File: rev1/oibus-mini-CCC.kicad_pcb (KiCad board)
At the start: 2 copper layers, 37 x 60 mm, 81 parts, among them J1 Conn_01x04_Female, J2 USB_B_Micro, J3 uavcan_5pins, J4 Conn_01x02_Female, P1 TC2030-MCP, Q1 DMG3415U-7, Q2 DMG3415U-7, Q3 DMG3415U-7, SW1 SW_Push, U1 AP2112K-3.3, U10 TPD3E001DRLR, U2 SAM-M8Q, U3 NINA-B311-00B, U4 MCP73831-2-OT, U5 MCP1624T, U6 SHT31-DIS-B, U7 TCAN330, U8 STM32F303CCTx, U9 DW01C-G, Y1 16M, Y2 32kHz

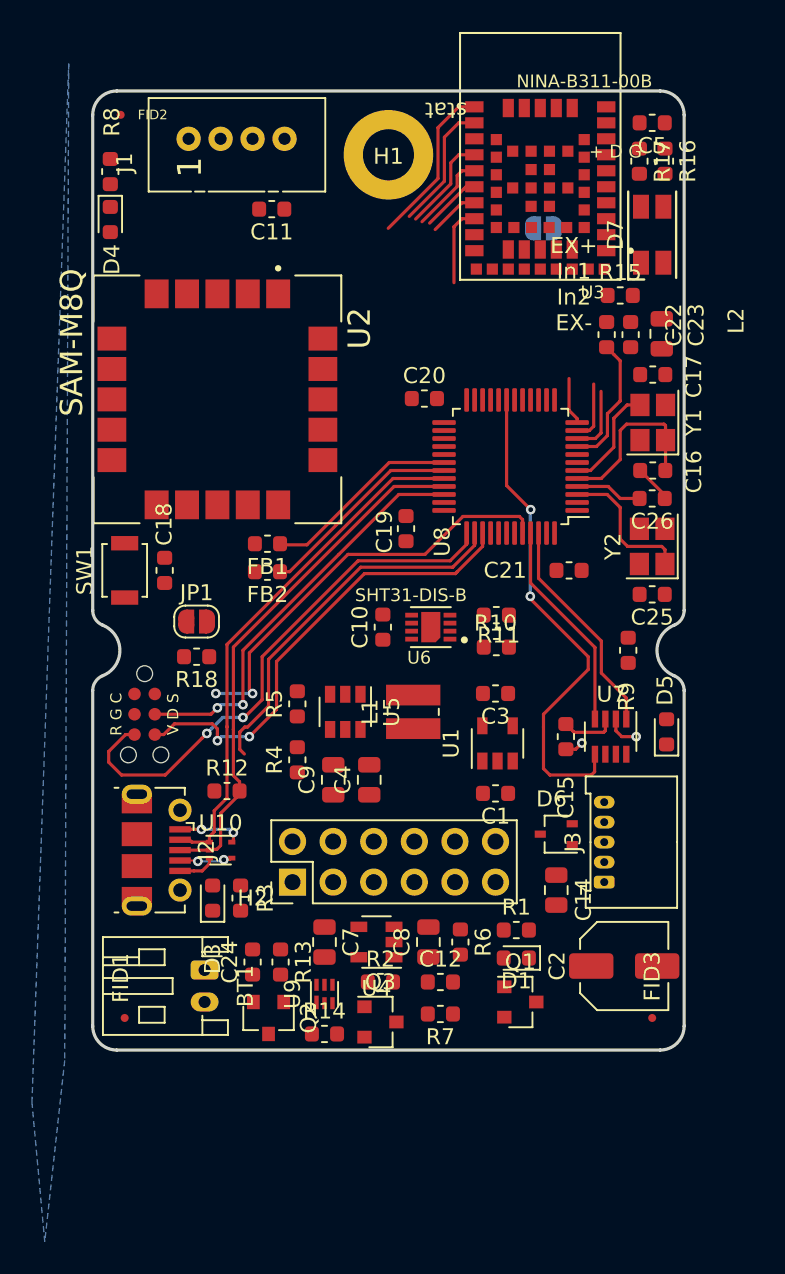
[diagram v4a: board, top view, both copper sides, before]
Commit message: routing halfway done
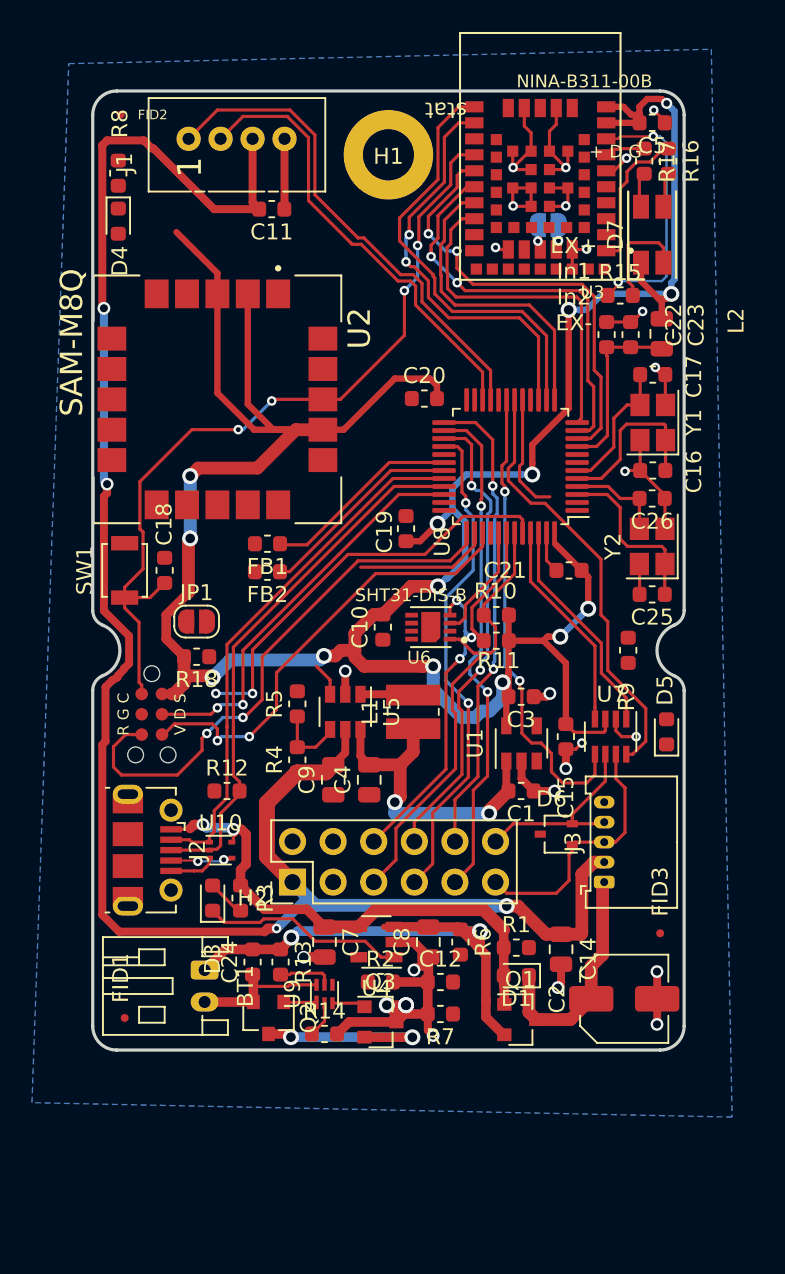
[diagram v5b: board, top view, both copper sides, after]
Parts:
- moved FID3 5.32 mm to (35.5, -7.30)
- moved C14 3.71 mm to (29.3, -6.30)
- moved C2 2.05 mm to (33.2, -3.20)
- moved R10 2.00 mm to (25.2, -27.2)
- moved C3 1.61 mm to (26.8, -22.1)
- moved C1 1.61 mm to (26.8, -16.2)
- moved R11 1.60 mm to (25.2, -25.6)
- moved U1 1.50 mm to (26.8, -19.2)
- moved Q1 1.10 mm to (26.8, -1.90)
- moved D1 1.10 mm to (26.5, -4.65)
- moved R1 1.10 mm to (26.5, -6.40)
- moved J2 0.56 mm to (3.44, -12.5)
- moved D4 0.51 mm to (1.60, -51.9)
- moved R8 0.51 mm to (1.60, -54.9)
- moved P1 0.45 mm to (3.70, -21.0)
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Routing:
- net +3V3: track 3.46 -> 185.2 mm, vias 0 -> 14
- net +5V: track 0.00 -> 118.5 mm, vias 0 -> 4
- net GND: track 8.08 -> 88.0 mm, vias 2 -> 26
- net /~RESET: track 5.91 -> 51.0 mm, vias 0 -> 4
- net /VIN: track 0.00 -> 34.5 mm, vias 0 -> 2
- net +BATT: track 0.00 -> 33.2 mm, vias 0 -> 2
- net /SPI_SCK: track 0.00 -> 31.7 mm, vias 0 -> 2
- net /SPI_MOSI: track 0.00 -> 31.2 mm, vias 0 -> 2
- net /SPS_RX: track 0.00 -> 31.1 mm
- net /~SPI_ADS_CS: track 0.00 -> 29.8 mm, vias 0 -> 2
- net /SPI_MISO: track 0.00 -> 29.5 mm, vias 0 -> 2
- net /SDA: track 0.00 -> 29.3 mm
- net /SPS_TX: track 0.00 -> 28.5 mm
- net VBUS: track 4.06 -> 32.4 mm
- net /SCL: track 0.00 -> 27.7 mm, vias 0 -> 3
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
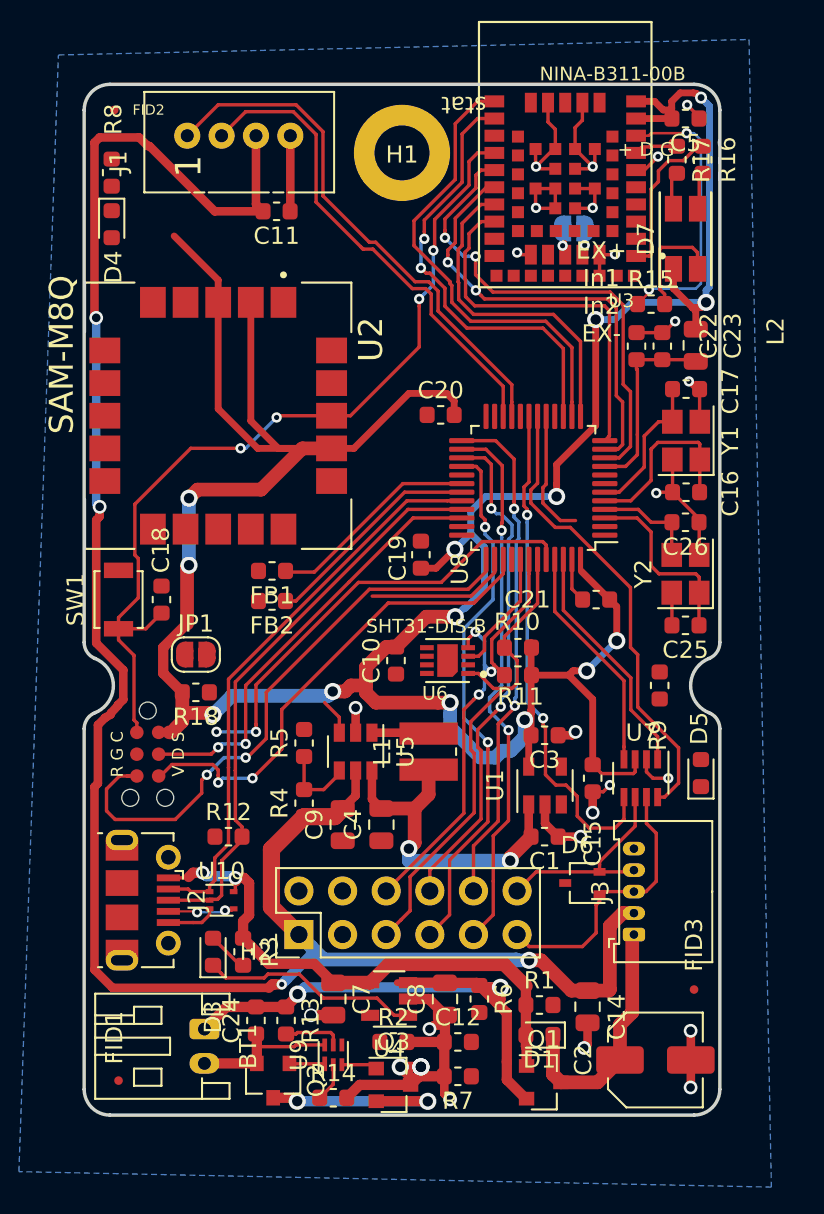
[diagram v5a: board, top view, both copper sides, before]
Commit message: finished routing, DRC clear
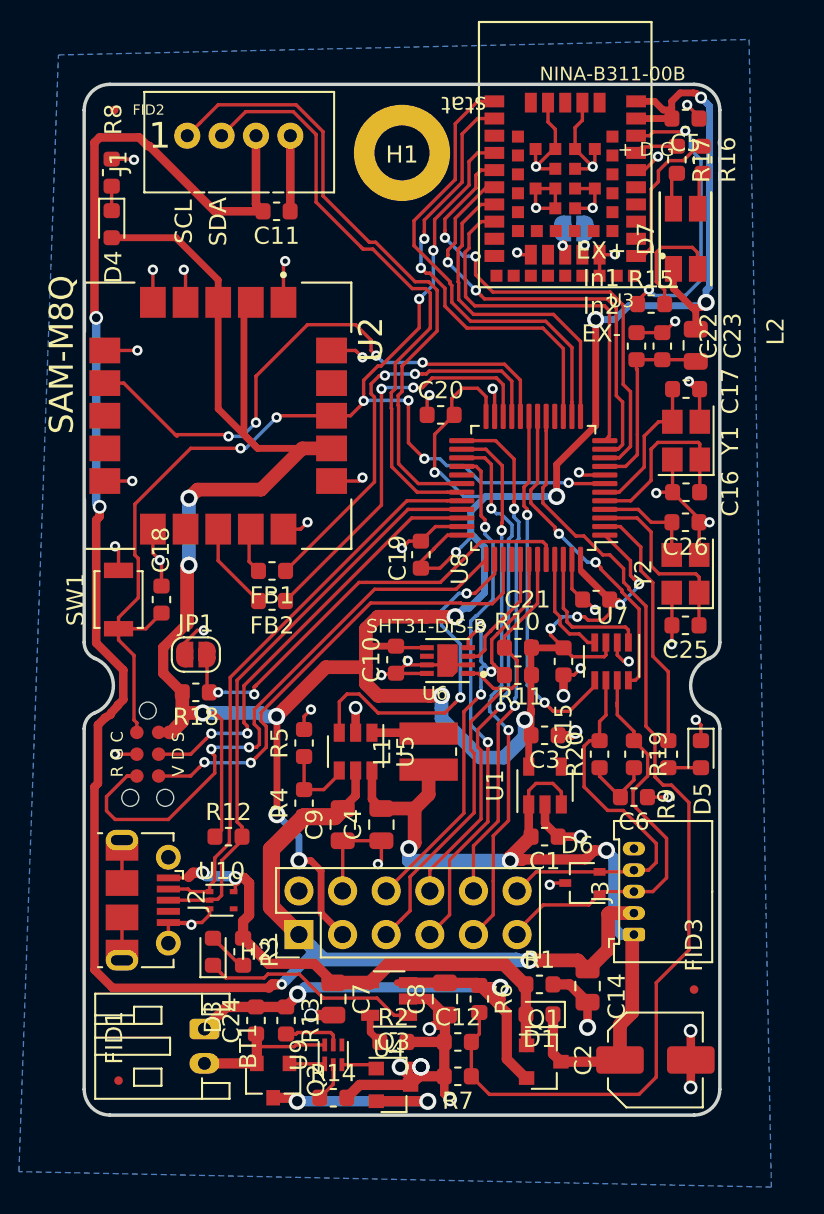
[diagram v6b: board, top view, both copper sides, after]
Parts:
- added C6: 100n, Capacitor_SMD:C_0603_1608Metric, F.Cu at (32.0, -18.5)
- added R19: 60R, Resistor_SMD:R_0603_1608Metric, F.Cu at (32.0, -21.0)
- added R20: 60R, Resistor_SMD:R_0603_1608Metric, F.Cu at (30.0, -21.0)
- moved C15 7.01 mm to (27.9, -26.4)
- moved U7 7.01 mm to (30.7, -26.4)
- moved R9 4.03 mm to (34.0, -21.0)
- moved C14 1.20 mm to (29.3, -7.50)
- moved Q1 1.20 mm to (26.8, -3.10)
- moved D1 1.20 mm to (26.5, -5.85)
- moved R1 1.20 mm to (26.5, -7.60)
- moved D5 1.10 mm to (35.9, -21.0), turned to 270 degrees
- moved C10 0.05 mm to (18.1, -26.5)
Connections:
- J1 pad 1: /SPS_RX -> SPS_RX
- J1 pad 2: /SPS_TX -> SPS_TX
- J2 pad 4: /ID -> (no net)
- U10 pad 4: /ID -> (no net)
- U6 pad 6: /~RESET -> (no net)
- U8 pad 2: (no net) -> /CAN_LED
- U8 pad 21: /SPS_RX -> GPS_RX
- U8 pad 22: /SPS_TX -> GPS_TX
- U8 pad 30: GPS_RX -> SPS_RX
- U8 pad 31: GPS_TX -> SPS_TX
- U8 pad 40: /CAN_LED -> (no net)
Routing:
- net GND: track 88.0 -> 151.8 mm, vias 26 -> 54
- net /BAT_MEAS: track 7.45 -> 59.2 mm
- net SPS_RX: track 0.00 -> 37.2 mm
- net SPS_TX: track 0.00 -> 35.3 mm
- net +3V3: track 185.2 -> 220.2 mm, vias 14 -> 19
- net /GPS_TIME: track 0.00 -> 33.7 mm, vias 0 -> 4
- net /SPS_RX: track 31.1 -> 0.00 mm
- net /SPS_TX: track 28.5 -> 0.00 mm
- net /~RESET: track 51.0 -> 68.6 mm, vias 4 -> 8
- net /VIN: track 34.5 -> 49.6 mm, vias 2 -> 3
- net /CAN_LED: track 0.00 -> 14.5 mm
- net GPS_RX: track 12.4 -> 23.9 mm, vias 0 -> 2
- net GPS_TX: track 12.9 -> 24.0 mm, vias 0 -> 2
- net /CAN_L: track 12.5 -> 22.5 mm
- net /5V_EN: track 10.6 -> 20.2 mm, vias 0 -> 2
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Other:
- board text added: "SCL"
- board text added: "SDA"

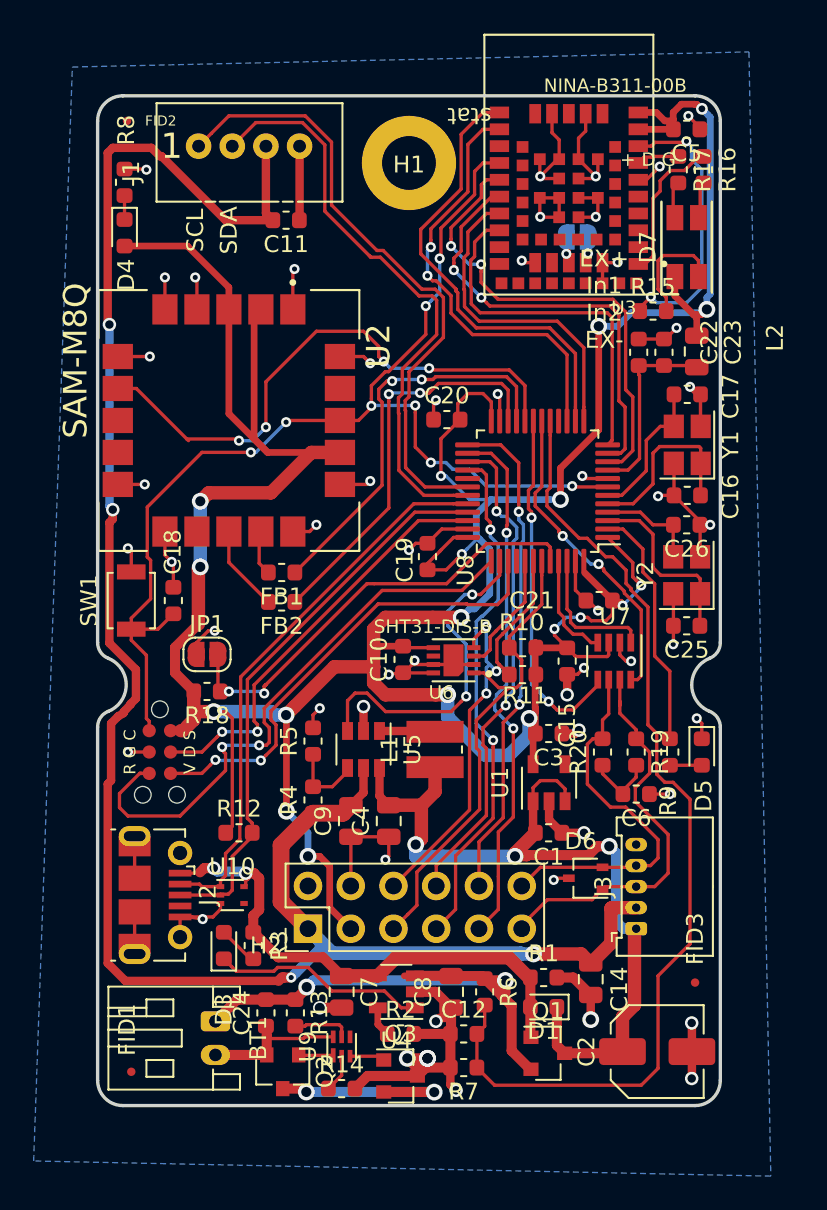
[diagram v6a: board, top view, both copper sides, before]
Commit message: Corrected Silkscreen, added CCC logo, OSH logo, License and revision and other labels
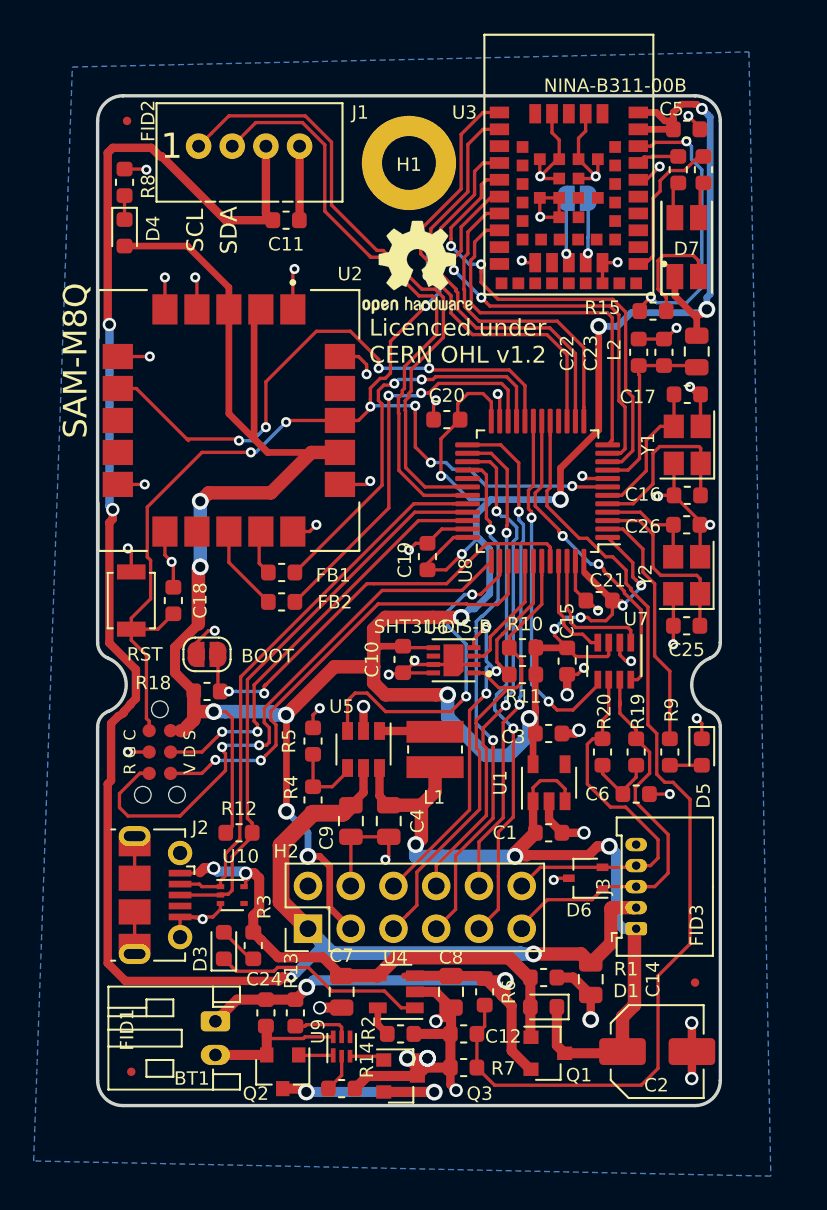
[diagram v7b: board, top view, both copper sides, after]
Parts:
- added G***: LOGO, lib_fp:CCC_logo, B.Cu at (18.1, -44.6)
- added REF**: OSHW-Logo2_7.3x6mm_SilkScreen, Symbol:OSHW-Logo2_7.3x6mm_SilkScreen, F.Cu at (19.0, -49.8)
- moved B1 12.6 mm to (18.9, -20.9)
- moved NFC 2.30 mm to (28.5, -53.9)
- renumbered JP1 to BOOT, J4 to NFC, SW1 to RST
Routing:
- net GND: track 151.8 -> 148.8 mm, vias 54 -> 53
- net Net-(J4-Pad2): track 1.99 -> 4.29 mm
- net Net-(J4-Pad1): track 1.59 -> 3.89 mm
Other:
- board text added: "5V"
- board text added: "<<MCU >>MCU"
- board text added: "Air Quality Sensor Board Made with KiCAD by Octanis Instruments OÜ www.octanis.ch"
- board text added: "BAT+"
- board text added: "GND"
- board text added: "GPS"
- board text added: "Licenced under CERN OHL v1.2"
- board text added: "Rev 1, 10.2019, RT For research purposes only, not approved for resale."
- board text added: "SPS30"
- board text added: "THE CLIMATE CITY CUP"
- board text removed: "+ D G"
- board text removed: "EX+ In1 In2 EX-"
- board text removed: "For prototyping purposes only, not approved for resale."
- board text removed: "OIBUS-Mini Load Cell Module Rev 1, 7.2019, RT Octanis Instruments OÜ www.octanis.ch"
- board text removed: "stat"
- board text removed: "← TagConnect SWD"

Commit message: performed some last fixes. Ready to review
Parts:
- removed BOOT: Jumper_NO_Small, Jumper:SolderJumper-2_P1.3mm_Open_RoundedPad1.0x1.5mm
- removed RST: SW_Push, Button_Switch_SMD:SW_SPST_B3U-1000P
- added SW1: SW_Push, Button_Switch_SMD:SW_SPST_B3U-1000P, F.Cu at (2.00, -30.0)
- D1: footprint Diode_SMD:D_0603_1608Metric -> Diode_SMD:D_SOD-123F
- Q2, Q3: value DMG3415U-7 -> NMOS
- moved R18 3.86 mm to (5.40, -28.3), turned to 0 degrees
- moved C18 3.52 mm to (5.40, -26.6), turned to 0 degrees
- moved C14 2.70 mm to (29.2, -10.2)
- moved D1 0.78 mm to (27.2, -5.50)
- moved Q1 0.70 mm to (26.8, -2.40)
- renumbered NFC to J4
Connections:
- Q3 pad 2: Net-(Q2-Pad3) -> GND
- Q3 pad 3: GND -> Net-(Q2-Pad3)
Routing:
- net +BATT: track 32.0 -> 39.3 mm
- net /BOOT: track 26.9 -> 34.2 mm
- net GND: track 148.8 -> 154.2 mm, vias 53 -> 56
- net Net-(Q2-Pad3): track 12.1 -> 8.48 mm
- net /~RESET: track 68.7 -> 71.9 mm
- net +5V: track 116.6 -> 114.9 mm
- net VBUS: track 31.3 -> 32.5 mm
- net /VIN: track 49.6 -> 50.5 mm
- added copper zone on F.Cu, net GND
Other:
- board text added: "Air Quality Sensor Board Made with KiCad by Octanis Instruments www.octanis.ch"
- board text added: "BOOT"
- board text removed: "Air Quality Sensor Board Made with KiCAD by Octanis Instruments OÜ www.octanis.ch"
